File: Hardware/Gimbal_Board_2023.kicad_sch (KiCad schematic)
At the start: 72 parts, among them J1 6P6C, J2 RJ45_LED_Shielded, Q1 Q_NMOS_GDS, Q2 Q_NMOS_GDS, Q3 Q_NMOS_GDS, Q4 Q_NMOS_GDS, Q5 Q_NMOS_GDS, Q6 Q_NMOS_GDS, Q7 Q_NMOS_GDS, SW1 SW_Push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

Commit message: Electrical Check Fix
Fixed Some lables
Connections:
- net GND: now also C2.2, J1.3, J2.8, J2.9
- net LED: now also J1.4, J2.10
- net RX+: now also J1.6, J2.4
- net RX-: now also J1.5, J2.6
- net TX+: now also J1.1, J2.1
- net TX-: now also J1.2, J2.3
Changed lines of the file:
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@@
     (effects (font (size 1.27 1.27)) (justify left bottom))
   )
-  (label "TX-" (at 278.13 61.595 90)
+  (label "TX-" (at 278.13 60.96 90)
     (effects (font (size 1.27 1.27)) (justify left bottom))
   )
-  (label "LED" (at 283.21 61.595 90)
+  (label "LED" (at 283.21 60.96 90)
     (effects (font (size 1.27 1.27)) (justify left bottom))
   )
-  (label "GND" (at 280.67 61.595 90)
+  (label "GND" (at 280.67 60.96 90)
     (effects (font (size 1.27 1.27)) (justify left bottom))
   )
-  (label "RX+" (at 288.29 61.595 90)
+  (label "RX+" (at 288.29 60.96 90)
     (effects (font (size 1.27 1.27)) (justify left bottom))
   )
-  (label "TX+" (at 275.59 61.595 90)
+  (label "TX+" (at 275.59 60.96 90)
     (effects (font (size 1.27 1.27)) (justify left bottom))
   )
-  (label "RX-" (at 285.75 61.595 90)
+  (label "RX-" (at 285.75 60.96 90)
     (effects (font (size 1.27 1.27)) (justify left bottom))
   )

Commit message: Added in PCB and started organizing
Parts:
- C1, C3: footprint (none) -> Capacitor_SMD:C_0201_0603Metric_Pad0.64x0.40mm_HandSolder
- Conn6, Conn7: footprint (none) -> MRDT_Connectors:MOLEX_SL_09_Horizontal
- Conn8: footprint (none) -> MRDT_Connectors:MOLEX_SL_03_Horizontal
- DG1, DG2: footprint (none) -> LED_SMD:LED_0603_1608Metric_Pad1.05x0.95mm_HandSolder
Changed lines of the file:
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@@
       (effects (font (size 1.524 1.524)) (justify left))
     )
-    (property "Footprint" "" (id 2) (at 325.12 212.09 0)
+    (property "Footprint" "MRDT_Connectors:MOLEX_SL_03_Horizontal" (id 2) (at 325.12 212.09 0)
       (effects (font (size 1.524 1.524)) hide)
     )
@@
     (property "Reference" "DG1" (id 0) (at 80.9625 40.64 0))
     (property "Value" "LED" (id 1) (at 80.9625 43.18 0))
-    (property "Footprint" "" (id 2) (at 82.55 46.99 0)
+    (property "Footprint" "LED_SMD:LED_0603_1608Metric_Pad1.05x0.95mm_HandSolder" (id 2) (at 82.55 46.99 0)
       (effects (font (size 1.27 1.27)) hide)
     )
@@
     (property "Reference" "C3" (id 0) (at 66.04 78.74 90))
     (property "Value" "10 uF" (id 1) (at 66.04 81.28 90))
-    (property "Footprint" "" (id 2) (at 69.85 82.8548 0)
+    (property "Footprint" "Capacitor_SMD:C_0201_0603Metric_Pad0.64x0.40mm_HandSolder" (id 2) (at 69.85 82.8548 0)
       (effects (font (size 1.27 1.27)) hide)
     )
@@
       (effects (font (size 1.524 1.524)) (justify left))
     )
-    (property "Footprint" "" (id 2) (at 325.12 191.77 0)
+    (property "Footprint" "MRDT_Connectors:MOLEX_SL_09_Horizontal" (id 2) (at 325.12 191.77 0)
       (effects (font (size 1.524 1.524)) hide)
     )
@@
     (property "Reference" "DG2" (id 0) (at 80.9625 71.12 0))
     (property "Value" "LED" (id 1) (at 80.9625 73.66 0))
-    (property "Footprint" "" (id 2) (at 82.55 77.47 0)
+    (property "Footprint" "LED_SMD:LED_0603_1608Metric_Pad1.05x0.95mm_HandSolder" (id 2) (at 82.55 77.47 0)
       (effects (font (size 1.27 1.27)) hide)
     )
@@
     (property "Reference" "C1" (id 0) (at 87.63 78.74 90))
     (property "Value" "10 uF" (id 1) (at 87.63 81.28 90))
-    (property "Footprint" "" (id 2) (at 91.44 82.8548 0)
+    (property "Footprint" "Capacitor_SMD:C_0201_0603Metric_Pad0.64x0.40mm_HandSolder" (id 2) (at 91.44 82.8548 0)
       (effects (font (size 1.27 1.27)) hide)
     )
@@
       (effects (font (size 1.524 1.524)) (justify left))
     )
-    (property "Footprint" "" (id 2) (at 325.12 166.37 0)
+    (property "Footprint" "MRDT_Connectors:MOLEX_SL_09_Horizontal" (id 2) (at 325.12 166.37 0)
       (effects (font (size 1.524 1.524)) hide)
     )
@@
     )
     (path "/d8c8e734-d44d-40d0-81e3-9c194ce23c32"
-      (reference "C1") (unit 1) (value "10 uF") (footprint "")
+      (reference "C1") (unit 1) (value "10 uF") (footprint "Capacitor_SMD:C_0201_0603Metric_Pad0.64x0.40mm_HandSolder")
     )
     (path "/6e1bbe8f-6823-4b42-9fdc-5d11472484e0"
@@
     )
     (path "/73abef37-c26c-4905-a0af-647ac60bbe58"
-      (reference "C3") (unit 1) (value "10 uF") (footprint "")
+      (reference "C3") (unit 1) (value "10 uF") (footprint "Capacitor_SMD:C_0201_0603Metric_Pad0.64x0.40mm_HandSolder")
     )
     (path "/2e1f949a-c773-4848-982b-0092fee09aa7"
@@
     )
     (path "/e712985c-7eb3-43f4-92ab-d1cf6f0741f0"
-      (reference "Conn6") (unit 1) (value "Molex_SL_09") (footprint "")
+      (reference "Conn6") (unit 1) (value "Molex_SL_09") (footprint "MRDT_Connectors:MOLEX_SL_09_Horizontal")
     )
     (path "/a3047c81-7bdb-4c5e-bd75-170361faab14"
-      (reference "Conn7") (unit 1) (value "Molex_SL_09") (footprint "")
+      (reference "Conn7") (unit 1) (value "Molex_SL_09") (footprint "MRDT_Connectors:MOLEX_SL_09_Horizontal")
     )
     (path "/11bfd70b-08a6-40a6-80bc-30ac28abb6c9"
-      (reference "Conn8") (unit 1) (value "Molex_SL_03") (footprint "")
+      (reference "Conn8") (unit 1) (value "Molex_SL_03") (footprint "MRDT_Connectors:MOLEX_SL_03_Horizontal")
     )
     (path "/2efdf2af-1cd9-4ea1-8da8-577ea0c613f7"
@@
     )
     (path "/16459c02-a982-434b-90fe-5c083126eed2"
-      (reference "DG1") (unit 1) (value "LED") (footprint "")
+      (reference "DG1") (unit 1) (value "LED") (footprint "LED_SMD:LED_0603_1608Metric_Pad1.05x0.95mm_HandSolder")
     )
     (path "/bcb76786-41d2-46cd-8eba-9713e41720b0"
-      (reference "DG2") (unit 1) (value "LED") (footprint "")
+      (reference "DG2") (unit 1) (value "LED") (footprint "LED_SMD:LED_0603_1608Metric_Pad1.05x0.95mm_HandSolder")
     )
     (path "/0b1b924b-b37f-4488-a7c0-24b98962bc4f"

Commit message: Ran an electrical rule check
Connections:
- net +3.3V: now also SW1.2; no longer SW1.1
- net Servo_1_SW: now also SW1.1; no longer SW1.2
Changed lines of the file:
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@@
     (pin "2")
   )
-  (symbol (lib_id "Switch:SW_Push") (at 33.02 162.56 0) (unit 1)
+  (symbol (lib_id "Switch:SW_Push") (at 33.02 162.56 0) (mirror y) (unit 1)
     (in_bom yes) (on_board yes)
     (property "Reference" "SW1" (id 0) (at 33.02 155.321 0))

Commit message: Footprint assignment for capacitors
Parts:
- C1, C3: footprint Capacitor_SMD:C_0201_0603Metric_Pad0.64x0.40mm_HandSolder -> Capacitor_SMD:C_0603_1608Metric_Pad1.08x0.95mm_HandSolder
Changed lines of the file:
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@@
     (property "Reference" "C3" (id 0) (at 66.04 78.74 90))
     (property "Value" "10 uF" (id 1) (at 66.04 81.28 90))
-    (property "Footprint" "Capacitor_SMD:C_0201_0603Metric_Pad0.64x0.40mm_HandSolder" (id 2) (at 69.85 82.8548 0)
+    (property "Footprint" "Capacitor_SMD:C_0603_1608Metric_Pad1.08x0.95mm_HandSolder" (id 2) (at 69.85 82.8548 0)
       (effects (font (size 1.27 1.27)) hide)
     )
@@
     (property "Reference" "C1" (id 0) (at 87.63 78.74 90))
     (property "Value" "10 uF" (id 1) (at 87.63 81.28 90))
-    (property "Footprint" "Capacitor_SMD:C_0201_0603Metric_Pad0.64x0.40mm_HandSolder" (id 2) (at 91.44 82.8548 0)
+    (property "Footprint" "Capacitor_SMD:C_0603_1608Metric_Pad1.08x0.95mm_HandSolder" (id 2) (at 91.44 82.8548 0)
       (effects (font (size 1.27 1.27)) hide)
     )
@@
     )
     (path "/d8c8e734-d44d-40d0-81e3-9c194ce23c32"
-      (reference "C1") (unit 1) (value "10 uF") (footprint "Capacitor_SMD:C_0201_0603Metric_Pad0.64x0.40mm_HandSolder")
+      (reference "C1") (unit 1) (value "10 uF") (footprint "Capacitor_SMD:C_0603_1608Metric_Pad1.08x0.95mm_HandSolder")
     )
     (path "/6e1bbe8f-6823-4b42-9fdc-5d11472484e0"
@@
     )
     (path "/73abef37-c26c-4905-a0af-647ac60bbe58"
-      (reference "C3") (unit 1) (value "10 uF") (footprint "Capacitor_SMD:C_0201_0603Metric_Pad0.64x0.40mm_HandSolder")
+      (reference "C3") (unit 1) (value "10 uF") (footprint "Capacitor_SMD:C_0603_1608Metric_Pad1.08x0.95mm_HandSolder")
     )
     (path "/2e1f949a-c773-4848-982b-0092fee09aa7"

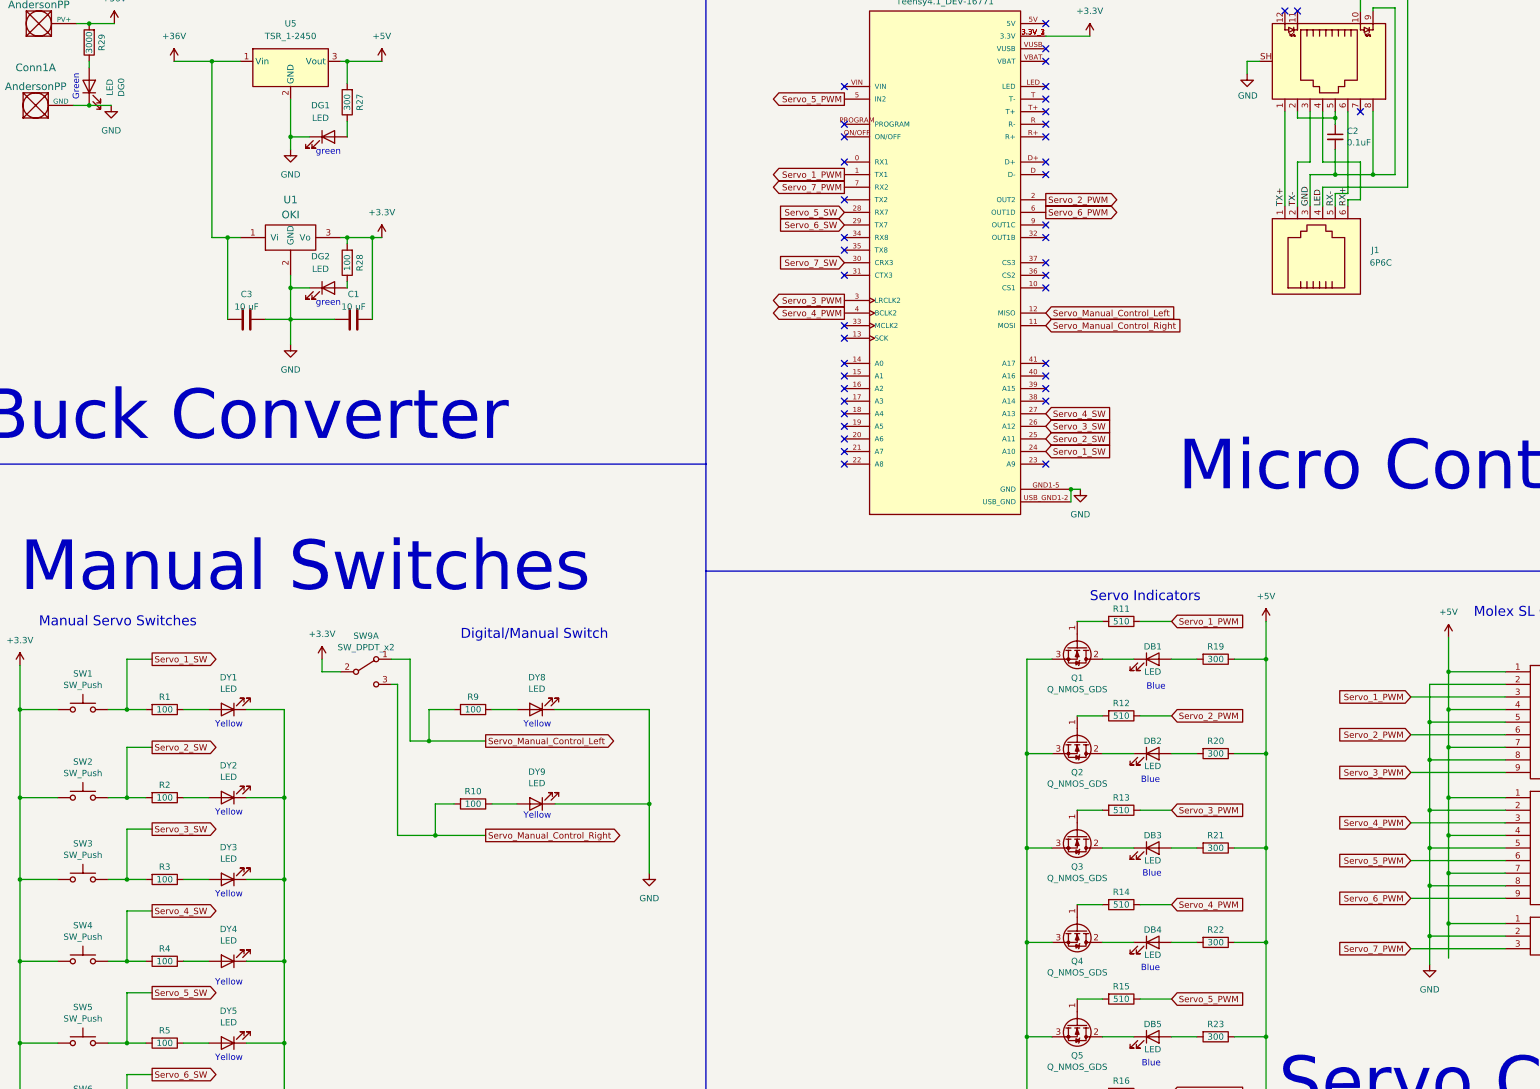
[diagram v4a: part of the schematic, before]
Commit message: Completed wiring and changed position of various pins
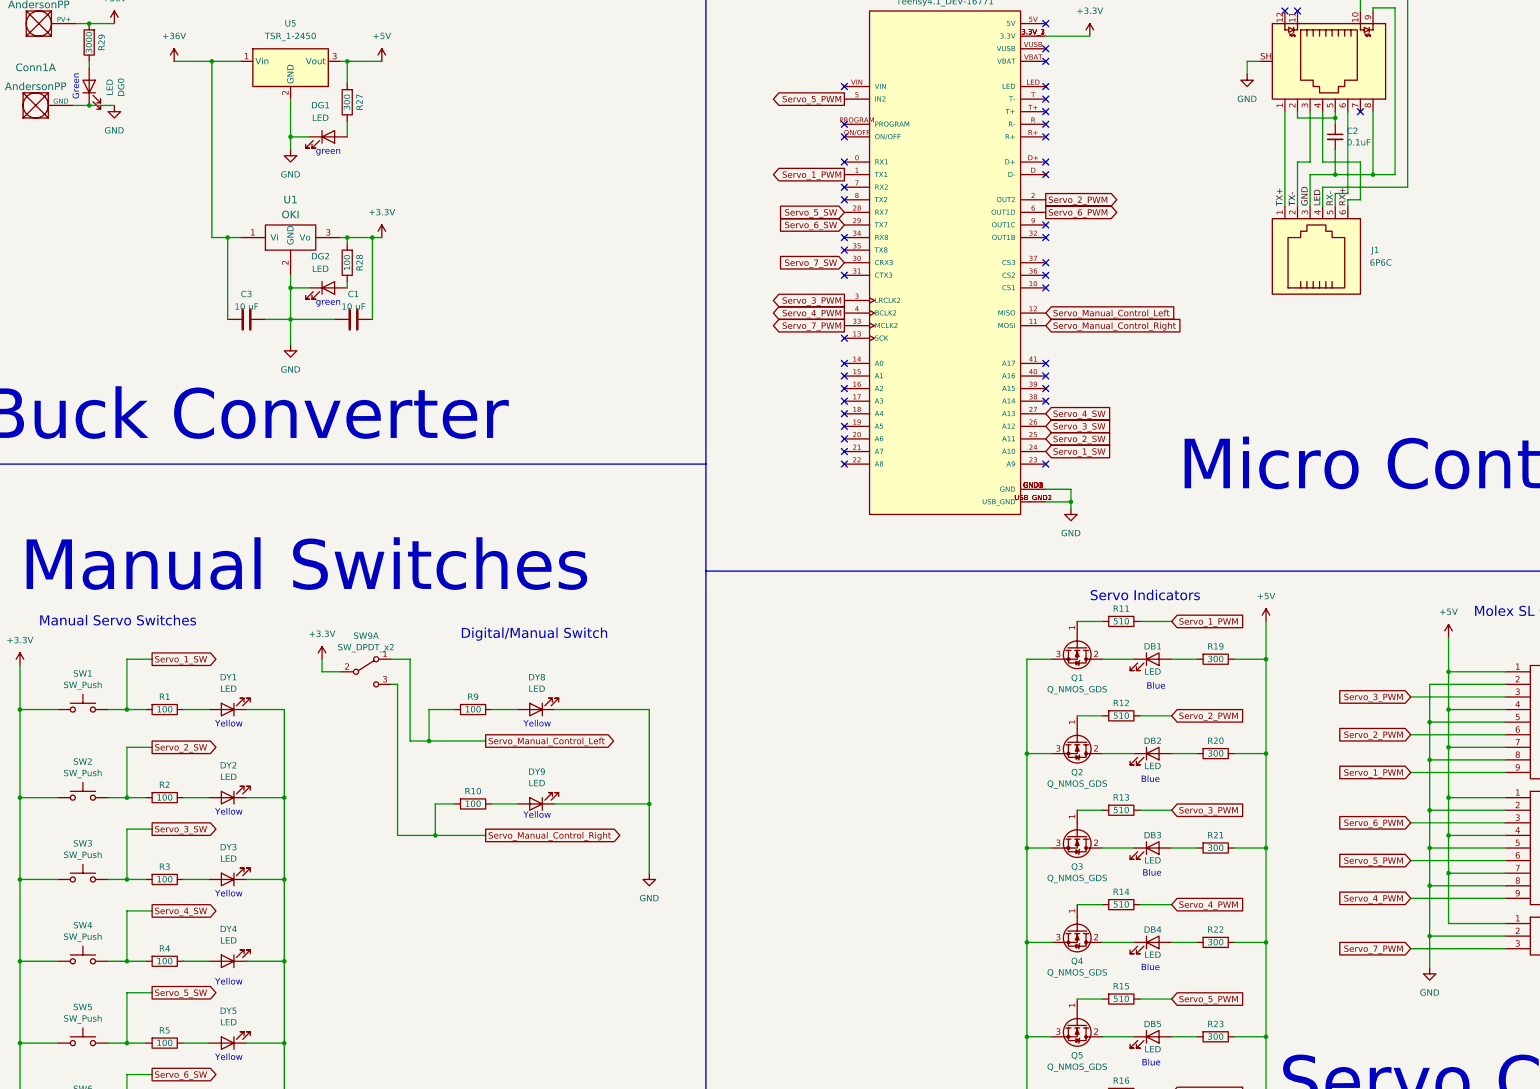
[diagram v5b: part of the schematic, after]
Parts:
- U3: footprint MRDT_Shields:Teensy_4_1_Vertical -> MODULE_DEV-16771
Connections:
- net GND: now also U3.GND1 (GND), U3.GND2 (GND), U3.GND3 (GND), U3.GND4 (GND), U3.GND5 (GND), U3.USB_GND1 (USB_GND), U3.USB_GND2 (USB_GND); no longer U3. (USB_GND), U3.GND1-5 (GND), U3.USB_GND1-2 (USB_GND)
- net Servo_1_PWM: now also Conn6.9; no longer Conn6.3
- net Servo_3_PWM: now also Conn6.3; no longer Conn6.9
- net Servo_4_PWM: now also Conn7.9; no longer Conn7.3
- net Servo_6_PWM: now also Conn7.3; no longer Conn7.9
- net Servo_7_PWM: now also U3.33 (MCLK2); no longer U3.7 (RX2)
